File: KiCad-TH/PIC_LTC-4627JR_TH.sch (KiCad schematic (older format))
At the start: 0 parts

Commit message: Stock components
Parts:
- added J?: Conn_01x05_Male, symbol Conn_01x05_Male
- added J?: Conn_01x04, symbol Conn_01x04
- added Q?: Q_NPN_EBC, symbol Q_NPN_EBC
- added R?: R, symbol R
- added U?: PIC16F18344-P, Housings_DIP:DIP-20_W7.62mm, symbol PIC16F18344-P
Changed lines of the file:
@@
 LIBS:contrib
 LIBS:valves
+LIBS:microchip_pic16mcu
+LIBS:leds
+LIBS:PIC_LTC-4627JR_TH-cache
 EELAYER 26 0
 EELAYER END
@@
 Comment4 ""
 $EndDescr
+$Comp
+L Conn_01x05_Male J?
+U 1 1 59CC3EBA
+P 1650 2650
+F 0 "J?" H 1756 3028 50  0000 C CNN
+F 1 "Conn_01x05_Male" H 1756 2937 50  0000 C CNN
+F 2 "" H 1650 2650 50  0001 C CNN
+F 3 "" H 1650 2650 50  0001 C CNN
+	1    1650 2650
+	1    0    0    -1
+$EndComp
+$Comp
+L Conn_01x04 J?
+U 1 1 59CC41F4
+P 1800 3900
+F 0 "J?" H 1880 3892 50  0000 L CNN
+F 1 "Conn_01x04" H 1880 3801 50  0000 L CNN
+F 2 "" H 1800 3900 50  0001 C CNN
+F 3 "" H 1800 3900 50  0001 C CNN
+	1    1800 3900
+	1    0    0    -1
+$EndComp
+$Comp
+L PIC16F18344-P U?
+U 1 1 59CC449B
+P 3500 2350
+F 0 "U?" H 3500 3228 50  0000 C CNN
+F 1 "PIC16F18344-P" H 3500 3137 50  0000 C CNN
+F 2 "Housings_DIP:DIP-20_W7.62mm" H 3500 1570 50  0001 C CNN
+F 3 "" H 3500 1650 50  0001 C CNN
+	1    3500 2350
+	1    0    0    -1
+$EndComp
+$Comp
+L R R?
+U 1 1 59CC458F
+P 5200 1200
+F 0 "R?" V 4993 1200 50  0000 C CNN
+F 1 "R" V 5084 1200 50  0000 C CNN
+F 2 "" V 5130 1200 50  0001 C CNN
+F 3 "" H 5200 1200 50  0001 C CNN
+	1    5200 1200
+	0    1    1    0
+$EndComp
+$Comp
+L Q_NPN_EBC Q?
+U 1 1 59CC48C7
+P 4300 4050
+F 0 "Q?" H 4491 4096 50  0000 L CNN
+F 1 "Q_NPN_EBC" H 4491 4005 50  0000 L CNN
+F 2 "" H 4500 4150 50  0001 C CNN
+F 3 "" H 4300 4050 50  0001 C CNN
+	1    4300 4050
+	1    0    0    -1
+$EndComp
 $EndSCHEMATC

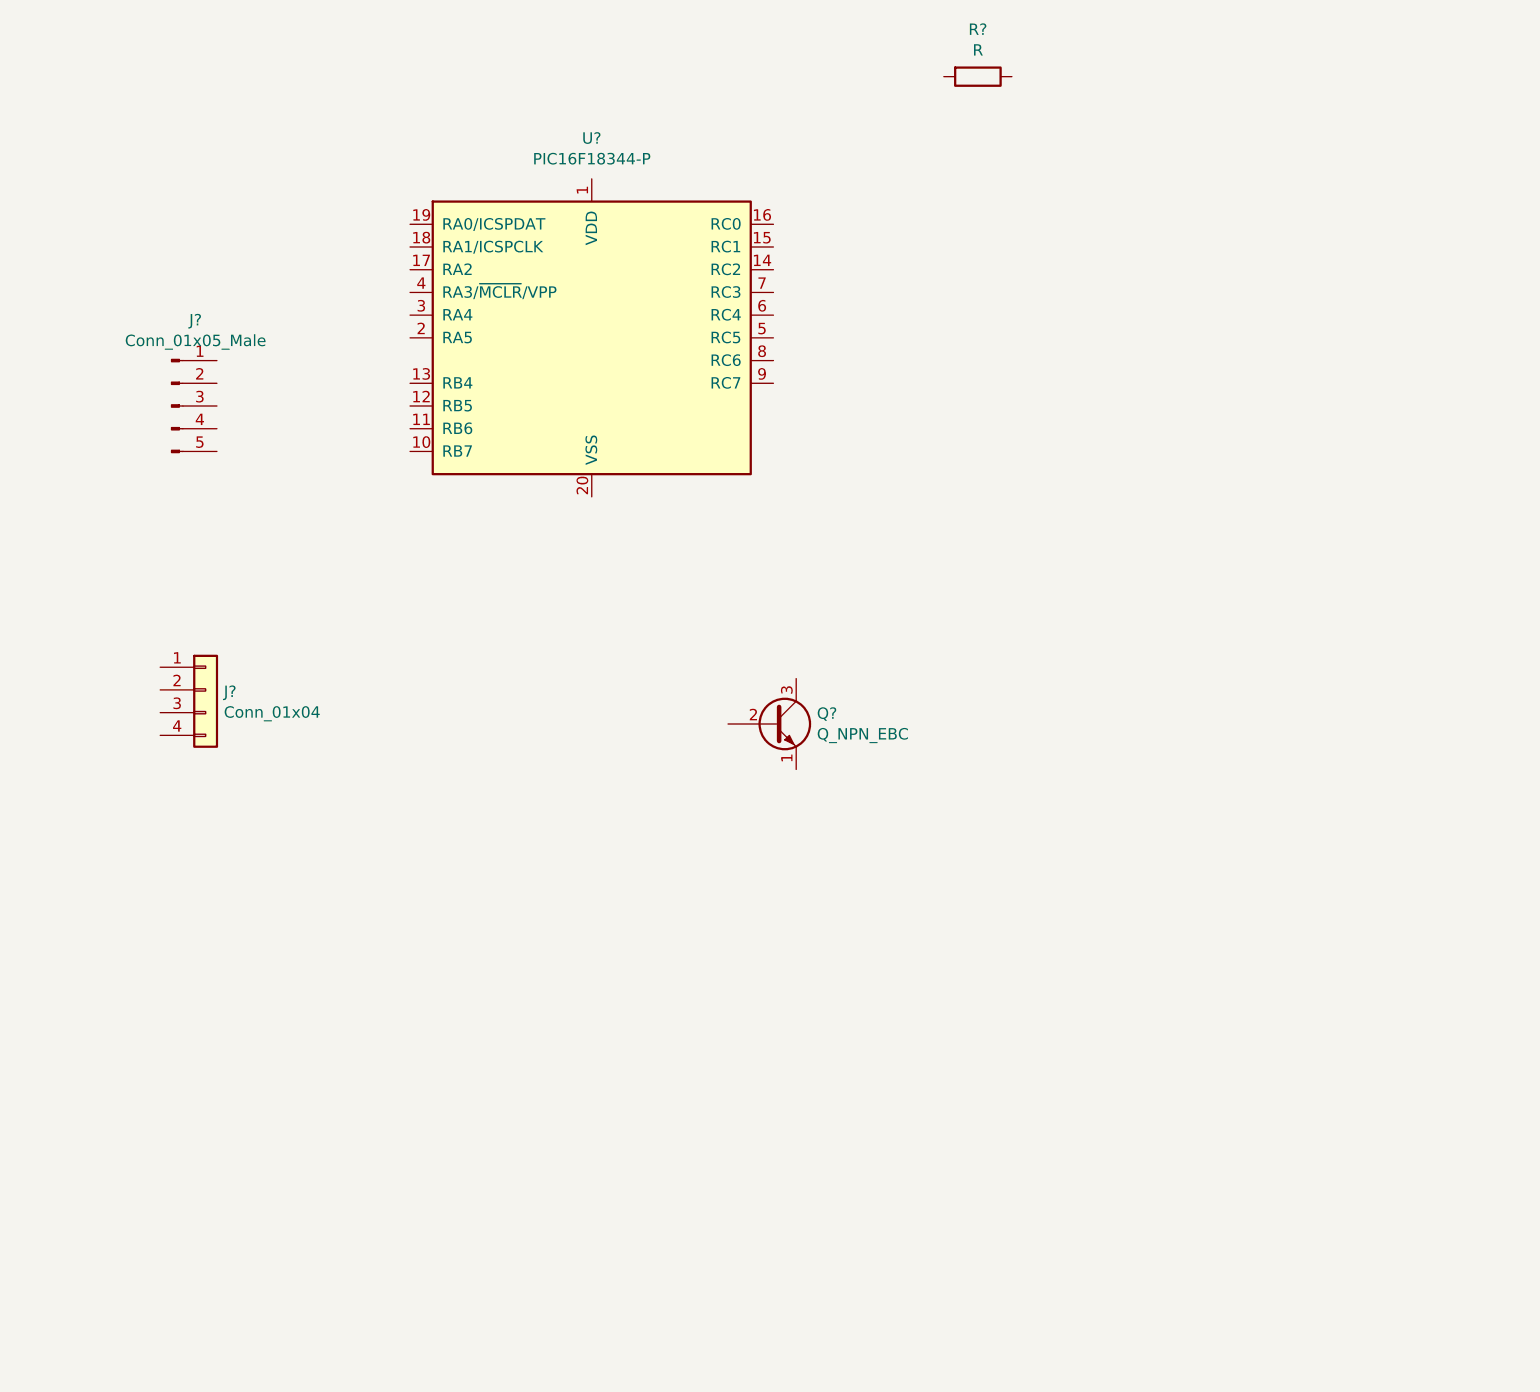
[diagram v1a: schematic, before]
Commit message: Wire up stock components
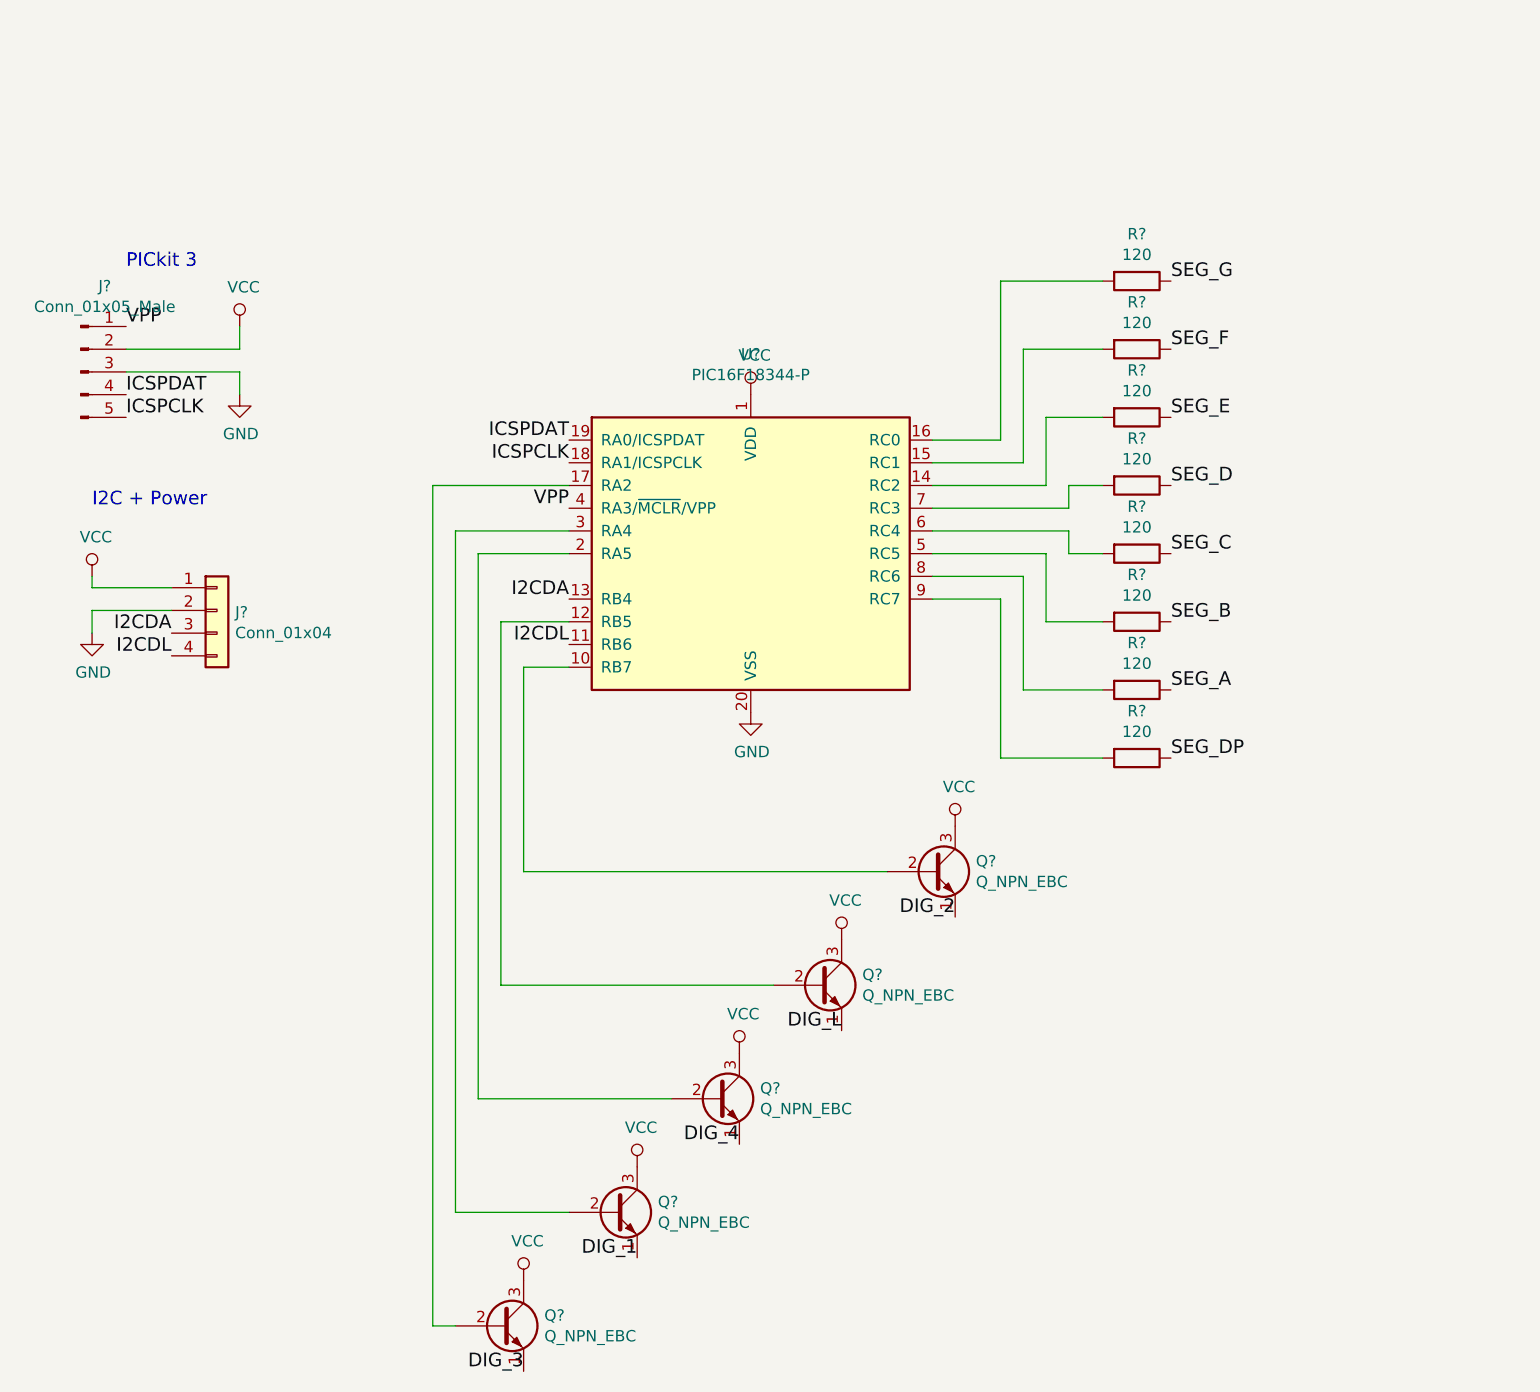
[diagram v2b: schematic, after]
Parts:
- added Q? (x4): Q_NPN_EBC, symbol Q_NPN_EBC
- added R? (x7): 120, symbol R
- R?: value R -> 120
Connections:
- net VPP: now reaches J?.1 (Pin_1)
- net VPP: now also U?.4 (RA3/~MCLR~/VPP)
- net VCC: now reaches J?.2 (Pin_2)
- net VCC: now also J?.1 (Pin_1), Q?.3 (C), U?.1 (VDD), Q?.3 (C), Q?.3 (C), Q?.3 (C), Q?.3 (C)
- net GND: now reaches J?.3 (Pin_3)
- net GND: now also J?.2 (Pin_2), U?.20 (VSS)
- net ICSPDAT: now reaches J?.4 (Pin_4)
- net ICSPDAT: now also U?.19 (RA0/ICSPDAT)
- net ICSPCLK: now reaches J?.5 (Pin_5)
- net ICSPCLK: now also U?.18 (RA1/ICSPCLK)
- net I2CDA: now reaches J?.3 (Pin_3)
- net I2CDA: now also U?.13 (RB4)
- net I2CDL: now reaches J?.4 (Pin_4)
- net I2CDL: now also U?.11 (RB6)
- net at U?.10 (RB7): now also Q?.2 (B)
- net at U?.12 (RB5): now also Q?.2 (B)
- net at U?.14 (RC2): now also R?.2
- net at U?.15 (RC1): now also R?.2
- net at U?.16 (RC0): now also R?.2
- net at U?.17 (RA2): now also Q?.2 (B)
- net at U?.2 (RA5): now also Q?.2 (B)
- net at U?.3 (RA4): now also Q?.2 (B)
- net at U?.5 (RC5): now also R?.2
- net at U?.6 (RC4): now also R?.2
- net at U?.7 (RC3): now also R?.2
- net at U?.8 (RC6): now also R?.2
- net at U?.9 (RC7): now also R?.2
- net SEG_G: now reaches R?.1
- net DIG_2: now reaches Q?.1 (E)
- new net DIG_1: Q?.1 (E)
- new net DIG_3: Q?.1 (E)
- new net DIG_4: Q?.1 (E)
- new net DIG_L: Q?.1 (E)
- new net SEG_A: R?.1
- new net SEG_B: R?.1
- new net SEG_C: R?.1
- new net SEG_D: R?.1
- new net SEG_DP: R?.1
- new net SEG_E: R?.1
- new net SEG_F: R?.1
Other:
- note added: "I2C + Power"
- note added: "PICkit 3"
- moved on the sheet: J?, Q?, R?, U?
